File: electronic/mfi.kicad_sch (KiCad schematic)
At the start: 17 parts, among them J1 RPi_GPIO, J4 TYPE-C-31-M-12, U1 MFI343S00177, U2 MFI337S3959, U3 MFI343S00177

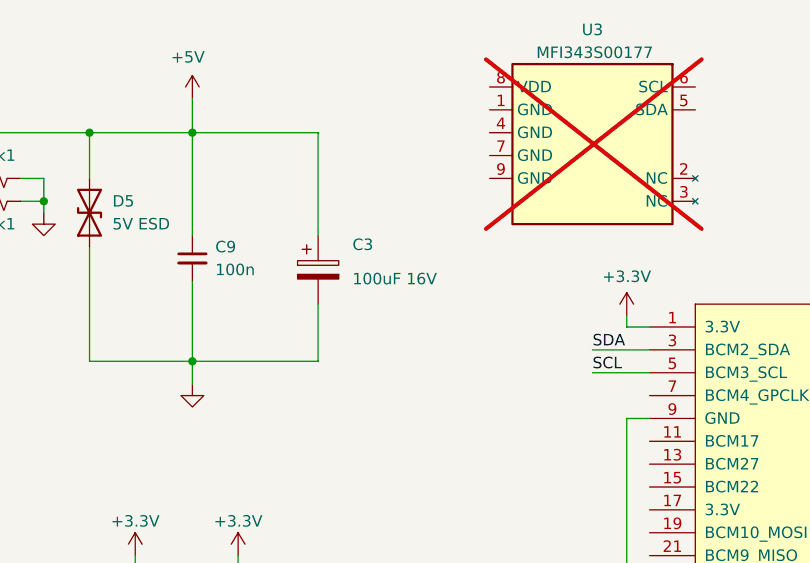
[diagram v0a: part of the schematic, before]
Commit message: Add bom
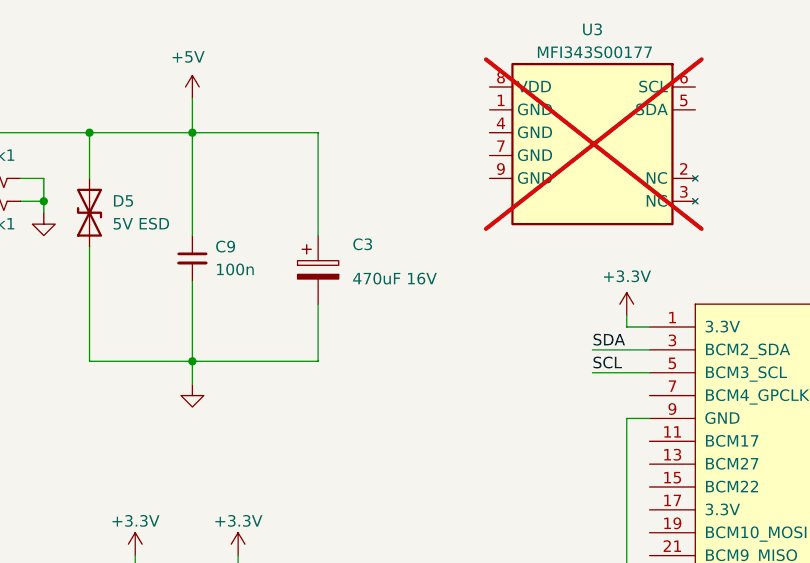
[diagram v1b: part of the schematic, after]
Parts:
- C3: value 100uF 16V -> 470uF 16V
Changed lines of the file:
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@@
 			)
 		)
-		(property "Value" "100uF 16V"
+		(property "Value" "470uF 16V"
 			(at 101.6 44.1959 0)
 			(effects
